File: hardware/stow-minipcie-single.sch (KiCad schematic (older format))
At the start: 9 parts

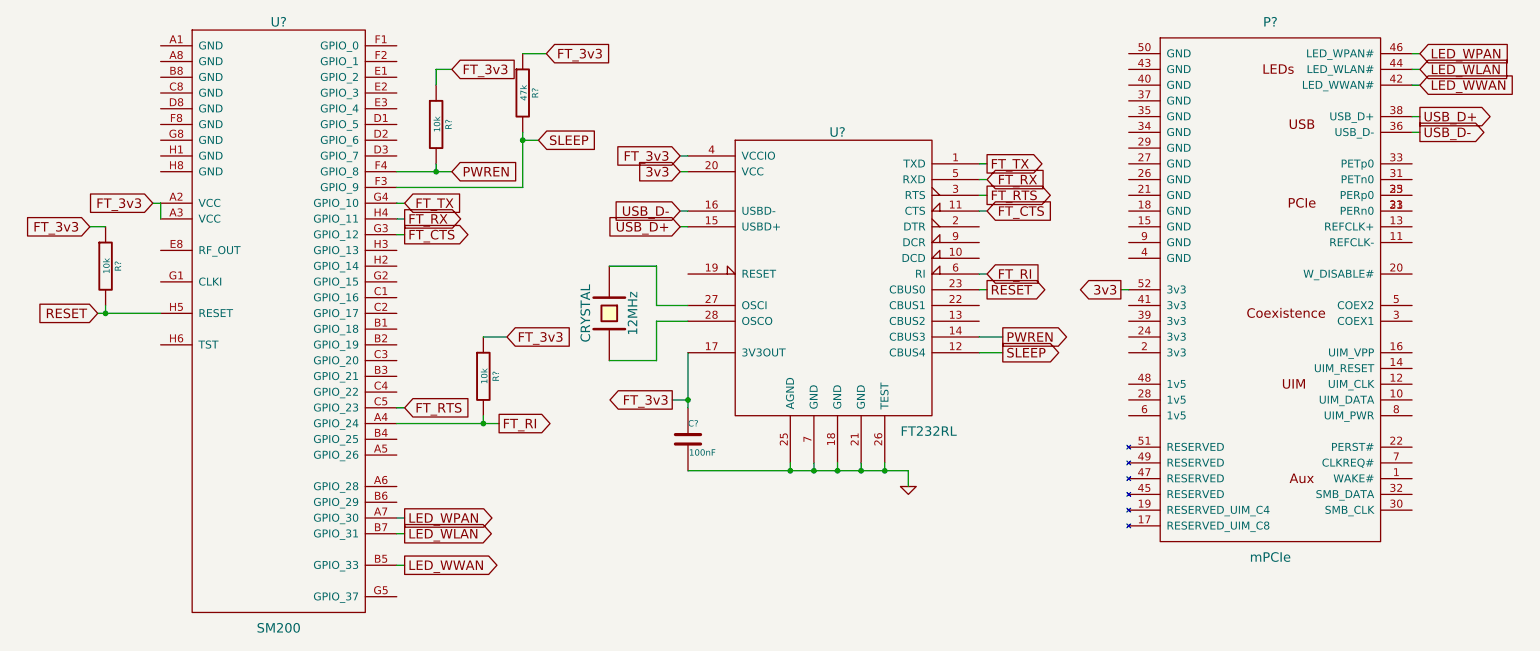
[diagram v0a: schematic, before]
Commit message: Wire up remaining GNDs and power.
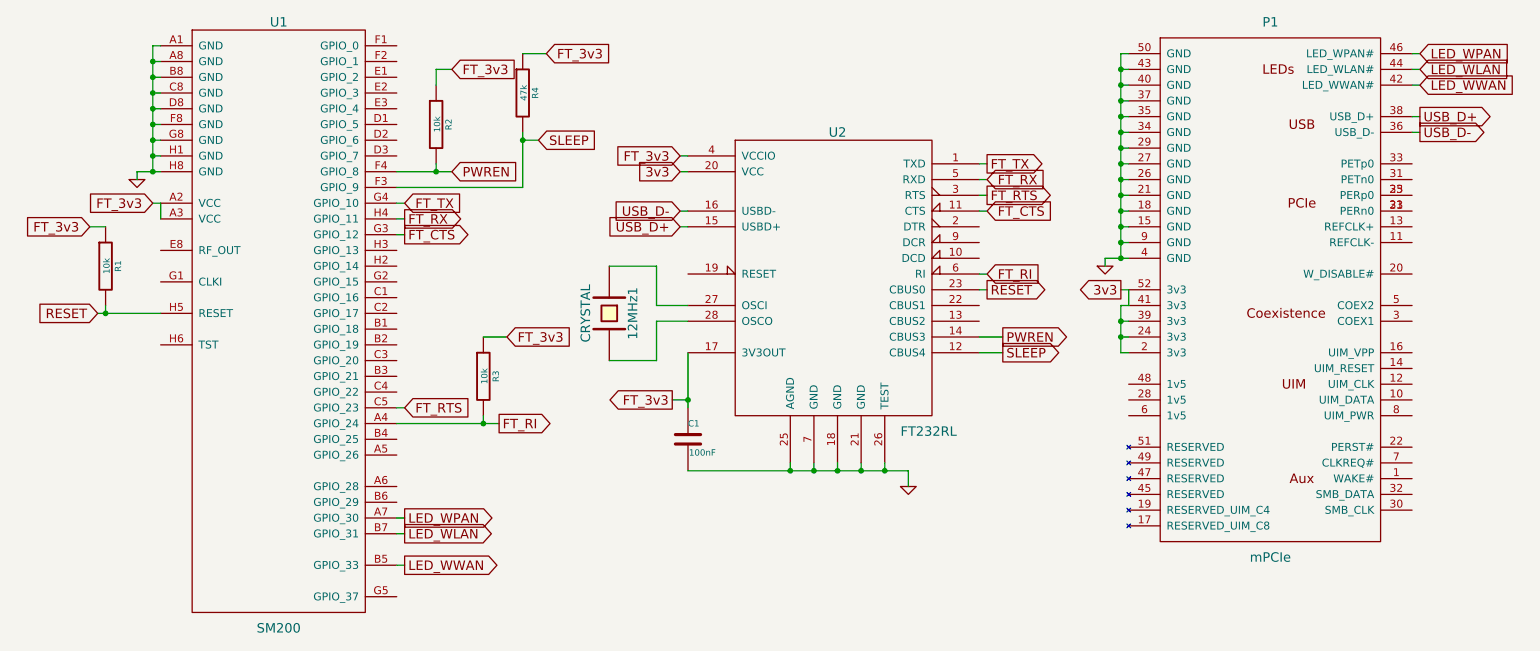
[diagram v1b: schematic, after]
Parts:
- gave numbers to parts that had none: 8
- renumbered 12MHz to 12MHz1
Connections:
- net 3v3: now also P1.2 (3v3), P1.24 (3v3), P1.39 (3v3), P1.41 (3v3)
- net GND: now also P1.15 (GND), P1.18 (GND), P1.21 (GND), P1.26 (GND), P1.27 (GND), P1.29 (GND), P1.34 (GND), P1.35 (GND), P1.37 (GND), P1.4 (GND), P1.40 (GND), P1.43 (GND), P1.50 (GND), P1.9 (GND), U1.A1 (GND), U1.A8 (GND), U1.B8 (GND), U1.C8 (GND), U1.D8 (GND), U1.F8 (GND), U1.G8 (GND), U1.H1 (GND), U1.H8 (GND)
